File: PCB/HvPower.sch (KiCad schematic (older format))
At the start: 34 parts

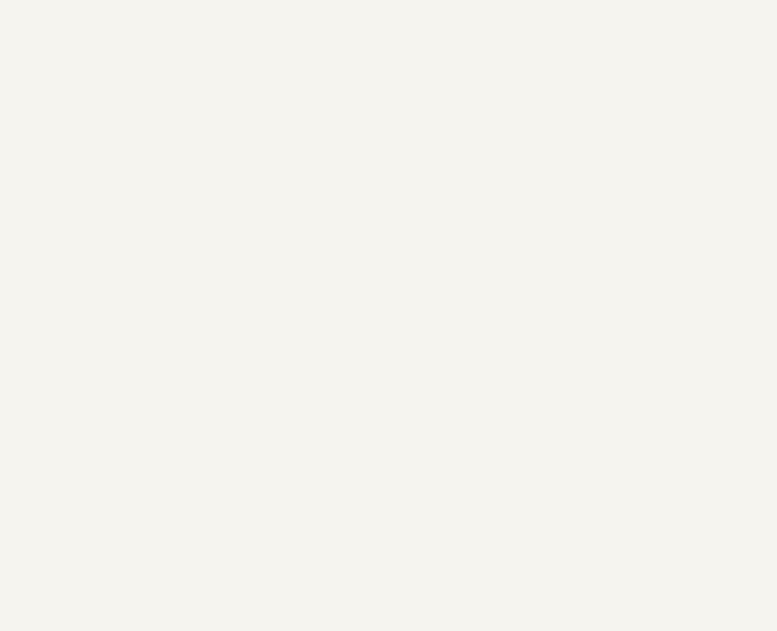
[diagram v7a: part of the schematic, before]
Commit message: Changed transmit-enable to connect to FPGA instead of microcontroller, added 10V linear regulator
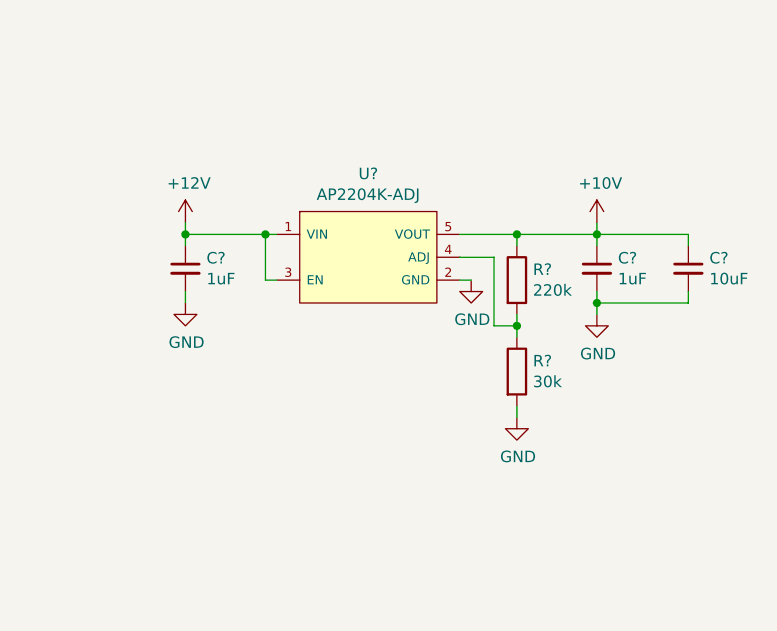
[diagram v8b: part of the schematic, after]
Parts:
- added C? (x2): 1uF, Capacitors_SMD:C_0805_HandSoldering, symbol Device:C_Small
- added C?: 10uF, Capacitors_SMD:C_1206_HandSoldering, symbol Device:C_Small
- added R?: 220k, Capacitors_SMD:C_0603_HandSoldering, symbol Device:R
- added R?: 30k, Capacitors_SMD:C_0603_HandSoldering, symbol Device:R
- added U?: AP2204K-ADJ, Parts:SOT23-5, symbol Parts:AP2204K-ADJ
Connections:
- net +12V: now also C?.1, U?.1 (VIN), U?.3 (EN)
- net GND: now also C?.2, C?.2, C?.2, R?.2, U?.2 (GND)
- new net: R?.1, R?.2, U?.4 (ADJ)
- new net +10V: C?.1, C?.1, R?.1, U?.5 (VOUT)
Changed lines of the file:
@@
 Wire Wire Line
 	5900 4750 5950 4750
+$Comp
+L Parts:AP2204K-ADJ U?
+U 1 1 5E0AC59D
+P 8950 3300
+F 0 "U?" H 8950 3665 50  0000 C CNN
+F 1 "AP2204K-ADJ" H 8950 3574 50  0000 C CNN
+F 2 "Parts:SOT23-5" H 8950 2950 50  0001 C CNN
+F 3 "https://www.diodes.com/part/view/AP2204" H 8950 2950 50  0001 C CNN
+	1    8950 3300
+	1    0    0    -1
+$EndComp
+$Comp
+L power:+12V #PWR?
+U 1 1 5E0AD6C7
+P 8150 3150
+F 0 "#PWR?" H 8150 3000 50  0001 C CNN
+F 1 "+12V" H 8165 3323 50  0000 C CNN
+F 2 "" H 8150 3150 50  0001 C CNN
+F 3 "" H 8150 3150 50  0001 C CNN
+	1    8150 3150
+	1    0    0    -1
+$EndComp
+$Comp
+L Device:C_Small C?
+U 1 1 5E0B5F92
+P 8150 3350
+F 0 "C?" H 8242 3396 50  0000 L CNN
+F 1 "1uF" H 8242 3305 50  0000 L CNN
+F 2 "Capacitors_SMD:C_0805_HandSoldering" H 8150 3350 50  0001 C CNN
+F 3 "https://www.digikey.ca/product-detail/en/samsung-electro-mechanics/CL21B105KAFNNNE/1276-1066-1-ND/3889152" H 8150 3350 50  0001 C CNN
+	1    8150 3350
+	1    0    0    -1
+$EndComp
+$Comp
+L Device:C_Small C?
+U 1 1 5E0B7046
+P 9950 3350
+F 0 "C?" H 10042 3396 50  0000 L CNN
+F 1 "1uF" H 10042 3305 50  0000 L CNN
+F 2 "Capacitors_SMD:C_0805_HandSoldering" H 9950 3350 50  0001 C CNN
+F 3 "https://www.digikey.ca/product-detail/en/samsung-electro-mechanics/CL21B105KAFNNNE/1276-1066-1-ND/3889152" H 9950 3350 50  0001 C CNN
+	1    9950 3350
+	1    0    0    -1
+$EndComp
+Wire Wire Line
+	8550 3400 8500 3400
+Wire Wire Line
+	8500 3400 8500 3200
+Wire Wire Line
+	8500 3200 8550 3200
+Wire Wire Line
+	8500 3200 8150 3200
+Wire Wire Line
+	8150 3200 8150 3150
+Connection ~ 8500 3200
+Wire Wire Line
+	8150 3200 8150 3250
+Connection ~ 8150 3200
+Wire Wire Line
+	8150 3500 8150 3450
+$Comp
+L power:GND #PWR?
+U 1 1 5E0CD1D0
+P 8150 3500
+F 0 "#PWR?" H 8150 3250 50  0001 C CNN
+F 1 "GND" H 8155 3327 50  0000 C CNN
+F 2 "" H 8150 3500 50  0001 C CNN
+F 3 "" H 8150 3500 50  0001 C CNN
+	1    8150 3500
+	1    0    0    -1
+$EndComp
+$Comp
+L power:+10V #PWR?
+U 1 1 5E0CFA90
+P 9950 3150
+F 0 "#PWR?" H 9950 3000 50  0001 C CNN
+F 1 "+10V" H 9965 3323 50  0000 C CNN
+F 2 "" H 9950 3150 50  0001 C CNN
+F 3 "" H 9950 3150 50  0001 C CNN
+	1    9950 3150
+	1    0    0    -1
+$EndComp
+Wire Wire Line
+	9950 3200 9950 3150
+Wire Wire Line
+	9950 3200 9950 3250
+Connection ~ 9950 3200
+Wire Wire Line
+	9350 3200 9600 3200
+$Comp
+L Device:R R?
+U 1 1 5E0E52C3
+P 9600 3400
+F 0 "R?" H 9670 3446 50  0000 L CNN
+F 1 "220k" H 9670 3355 50  0000 L CNN
+F 2 "Capacitors_SMD:C_0603_HandSoldering" V 9530 3400 50  0001 C CNN
+F 3 "https://www.digikey.ca/product-detail/en/stackpole-electronics-inc/RMCF0603FT220K/RMCF0603FT220KCT-ND/2417988" H 9600 3400 50  0001 C CNN
+	1    9600 3400
+	1    0    0    -1
+$EndComp
+$Comp
+L Device:R R?
+U 1 1 5E0E587B
+P 9600 3800
+F 0 "R?" H 9670 3846 50  0000 L CNN
+F 1 "30k" H 9670 3755 50  0000 L CNN
+F 2 "Capacitors_SMD:C_0603_HandSoldering" V 9530 3800 50  0001 C CNN
+F 3 "https://www.digikey.ca/product-detail/en/stackpole-electronics-inc/RMCF0603FT30K0/RMCF0603FT30K0CT-ND/1943086" H 9600 3800 50  0001 C CNN
+	1    9600 3800
+	1    0    0    -1
+$EndComp
+Wire Wire Line
+	9600 3250 9600 3200
+Connection ~ 9600 3200
+Wire Wire Line
+	9600 3200 9950 3200
+Wire Wire Line
+	9350 3300 9500 3300
+Wire Wire Line
+	9500 3300 9500 3600
+Wire Wire Line
+	9500 3600 9600 3600
+Wire Wire Line
+	9600 3600 9600 3550
+Wire Wire Line
+	9600 3600 9600 3650
+Connection ~ 9600 3600
+Wire Wire Line
+	9350 3400 9400 3400
+Wire Wire Line
+	9600 4000 9600 3950
+$Comp
+L power:GND #PWR?
+U 1 1 5E0FC5E1
+P 9950 3550
+F 0 "#PWR?" H 9950 3300 50  0001 C CNN
+F 1 "GND" H 9955 3377 50  0000 C CNN
+F 2 "" H 9950 3550 50  0001 C CNN
+F 3 "" H 9950 3550 50  0001 C CNN
+	1    9950 3550
+	1    0    0    -1
+$EndComp
+Wire Wire Line
+	9950 3550 9950 3500
+$Comp
+L power:GND #PWR?
+U 1 1 5E101152
+P 9600 4000
+F 0 "#PWR?" H 9600 3750 50  0001 C CNN
+F 1 "GND" H 9605 3827 50  0000 C CNN
+F 2 "" H 9600 4000 50  0001 C CNN
+F 3 "" H 9600 4000 50  0001 C CNN
+	1    9600 4000
+	1    0    0    -1
+$EndComp
+$Comp
+L power:GND #PWR?
+U 1 1 5E1017EA
+P 9400 3400
+F 0 "#PWR?" H 9400 3150 50  0001 C CNN
+F 1 "GND" H 9405 3227 50  0000 C CNN
+F 2 "" H 9400 3400 50  0001 C CNN
+F 3 "" H 9400 3400 50  0001 C CNN
+	1    9400 3400
+	1    0    0    -1
+$EndComp
+$Comp
+L Device:C_Small C?
+U 1 1 5E1058BA
+P 10350 3350
+F 0 "C?" H 10442 3396 50  0000 L CNN
+F 1 "10uF" H 10442 3305 50  0000 L CNN
+F 2 "Capacitors_SMD:C_1206_HandSoldering" H 10350 3350 50  0001 C CNN
+F 3 "https://www.digikey.ca/product-detail/en/kemet/C1206C106M3PACTU/399-8153-1-ND/3471876" H 10350 3350 50  0001 C CNN
+	1    10350 3350
+	1    0    0    -1
+$EndComp
+Wire Wire Line
+	9950 3200 10350 3200
+Wire Wire Line
+	10350 3200 10350 3250
+Wire Wire Line
+	9950 3500 10350 3500
+Wire Wire Line
+	10350 3500 10350 3450
+Connection ~ 9950 3500
+Wire Wire Line
+	9950 3500 9950 3450
 $EndSCHEMATC
